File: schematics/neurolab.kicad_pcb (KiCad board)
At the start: 2 copper layers, 127 x 53.6 mm, 170 parts, among them J1 GS3, J10 GS3, J12 GS3, J13 GS3, J14 GS3, J15 GS3, J16 Channel, J17 External, J18 USB_OTG, J19 GS3, J2 GS3, J20 GS2, J21 GS2, J22 GS2, J23 GS2, J24 GS2, J25 GS2, J26 ICSP Port, J27 GS2, J28 GS2, J3 GS3, J30 GS3, J31 GS3, J32 Bluetooth, J33 Reset Select, J34 GS2, J4 GS2, J5 GS2, J6 GS3, J7 GS3, J8 PowerOut, J9 GS3, Q1 2N7002, U1 ADP1720ARMZ-5, U10 OPA2111KP, U11 AD8422ARMZ, U12 OP4117, U13 OPA2111KP, U14 AD8422ARMZ, U15 OP4117, U16 AD7173, U17 ADR445BR, U18 Arduino, U2 ADP1720ARMZ-3.3, U3 AD8475, U4 AD8475, U5 MAX7480ESA+, U6 MAX7480ESA+, U7 MAX7480ESA+, U8 MAX7480ESA+, U9 TLC555CD, Y1 FA-20H

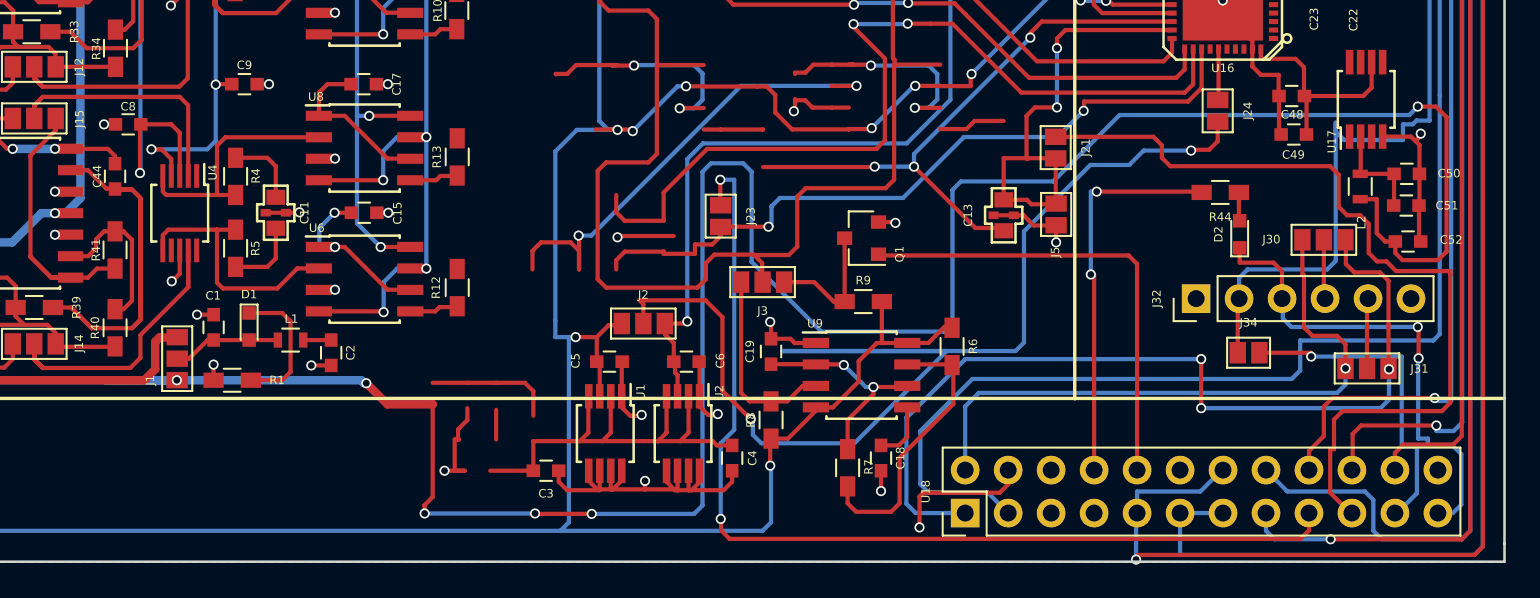
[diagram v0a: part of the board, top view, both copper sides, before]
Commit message: optimize: component placement
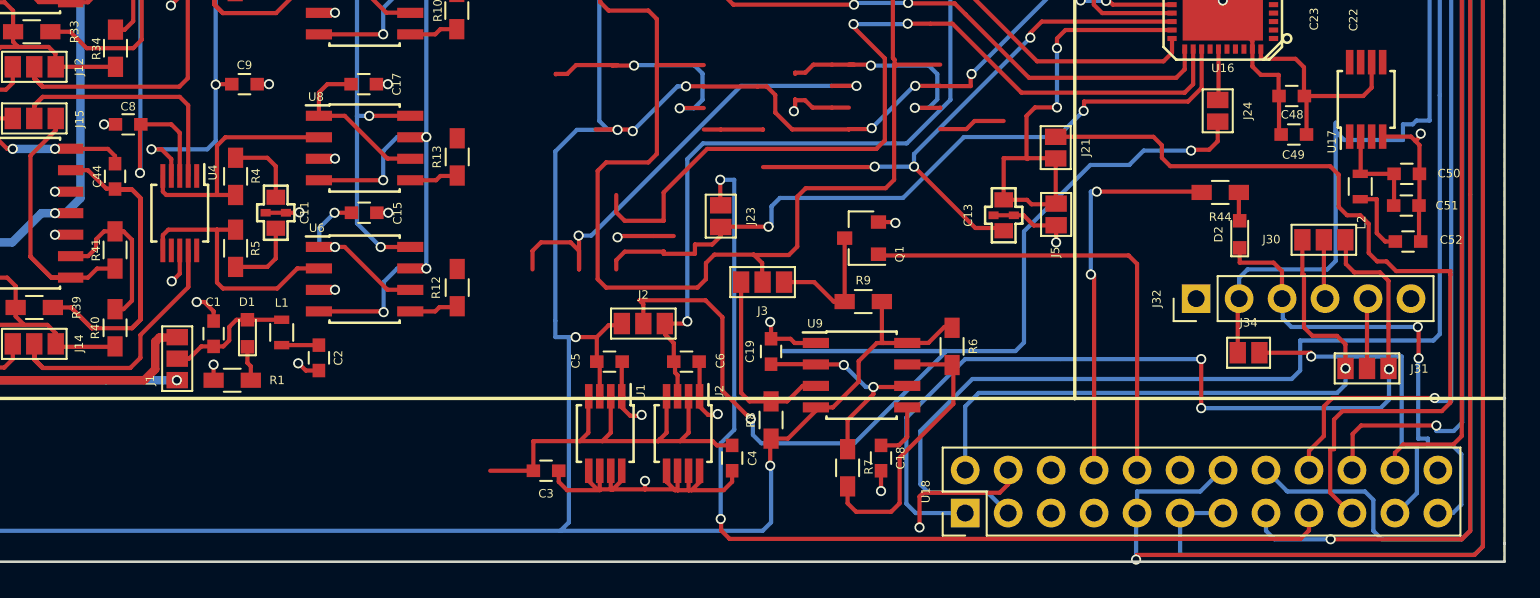
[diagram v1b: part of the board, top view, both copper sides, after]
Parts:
- moved C2 0.78 mm to (146.9, 113.8)
- moved L1 0.69 mm to (144.7, 112.3), turned to 270 degrees
- moved D1 0.41 mm to (142.7, 112.4), turned to 90 degrees
- moved C1 0.38 mm to (140.7, 112.4)
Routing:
- net +5.5V: track 187.0 -> 50.1 mm, vias 7 -> 2
- net (no net): track 140.0 -> 124.6 mm, vias 14 -> 13
- net Net-(D1-Pad1): track 8.19 -> 2.06 mm
- net Net-(C1-Pad1): track 6.41 -> 7.60 mm
- net GND: track 241.8 -> 242.9 mm
- net /External Power/VIN: track 29.4 -> 30.0 mm

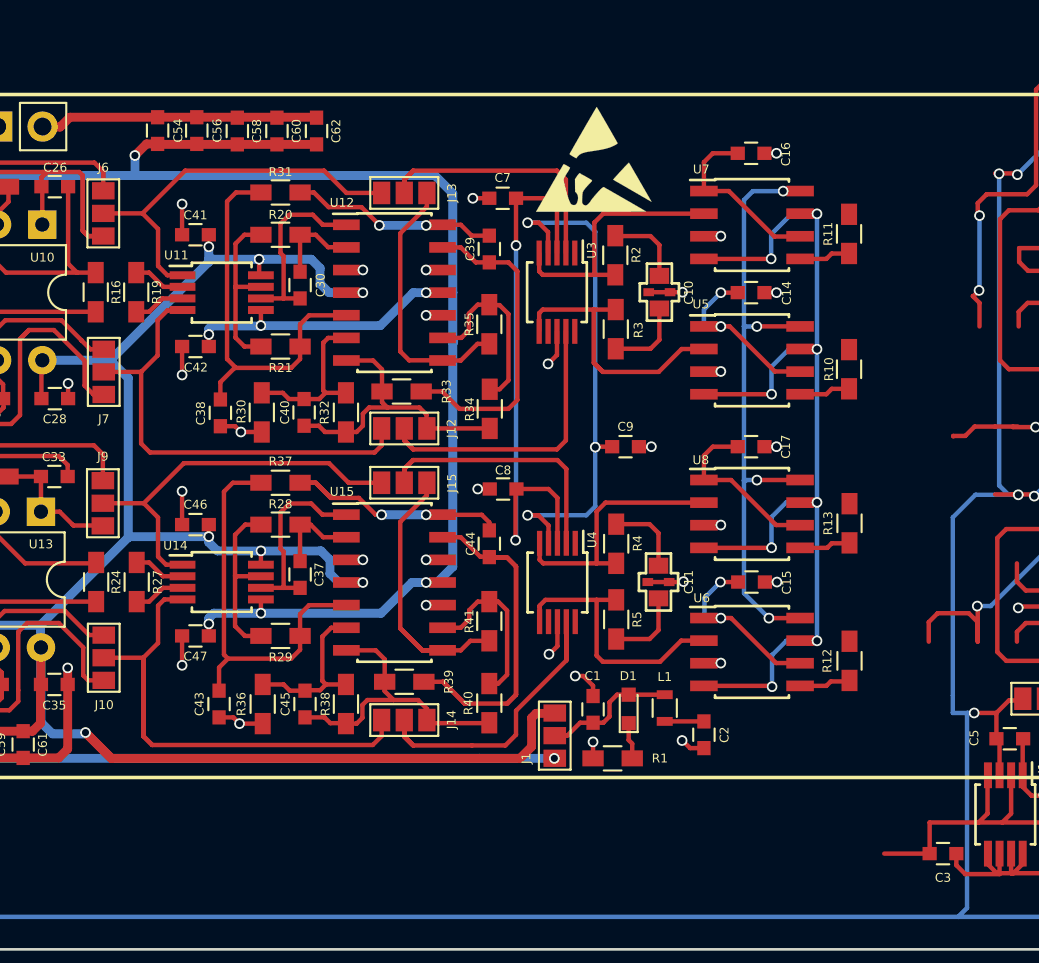
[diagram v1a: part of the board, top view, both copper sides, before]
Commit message: optimize: reduce spacing 20mils
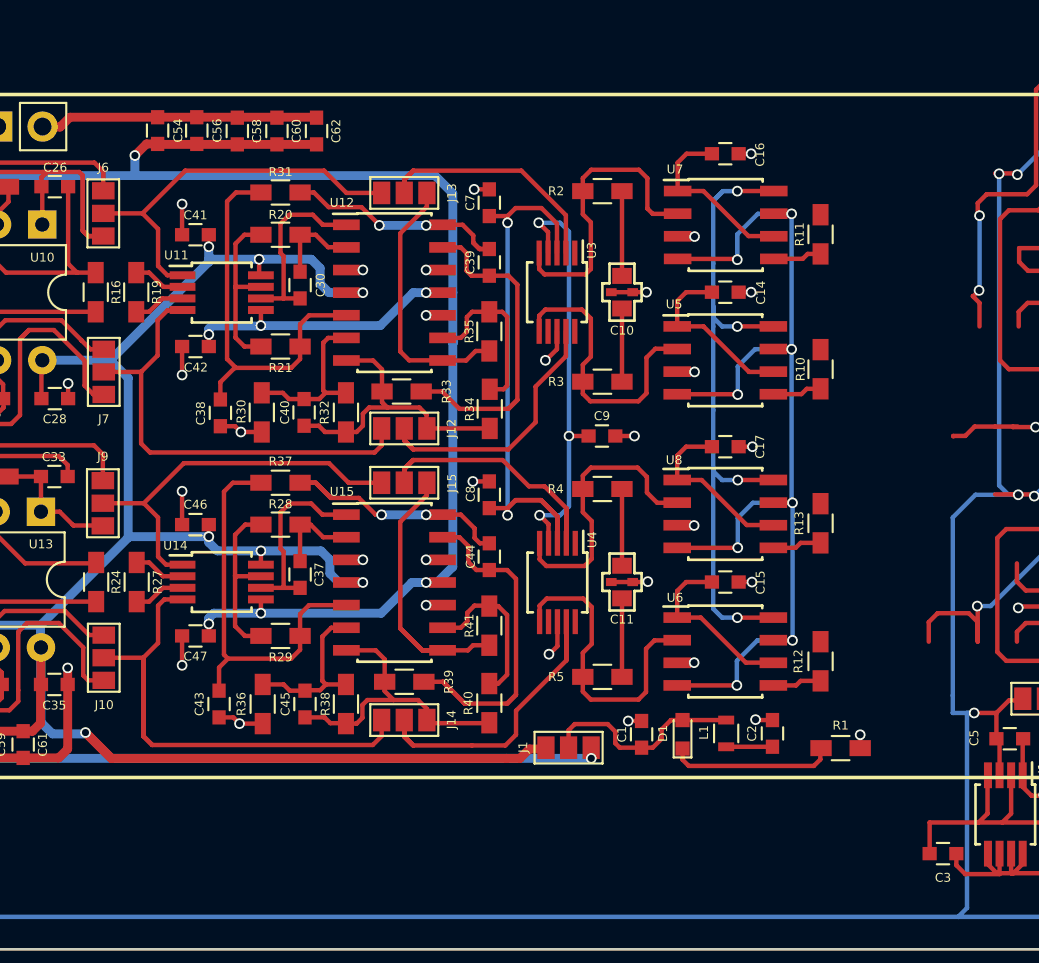
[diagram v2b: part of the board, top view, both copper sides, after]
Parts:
- removed REF***: ESD-Logo_6.6x6mm_SilkScreen, Symbols:ESD-Logo_6.6x6mm_SilkScreen
- moved R1 12.8 mm to (154.6, 114.6), turned to 0 degrees
- moved C2 3.85 mm to (150.8, 113.8), turned to 90 degrees
- moved L1 3.73 mm to (148.2, 113.8)
- moved R2 3.67 mm to (141.2, 83.3), turned to 180 degrees
- moved D1 3.34 mm to (145.7, 113.8)
- moved R5 3.32 mm to (141.2, 110.6), turned to 180 degrees
- moved R4 3.17 mm to (141.2, 100.0), turned to 180 degrees
- moved C1 3.06 mm to (143.4, 113.8)
- moved R3 3.04 mm to (141.2, 94.0), turned to 180 degrees
- moved C10 2.10 mm to (142.3, 89.0)
- moved C11 2.05 mm to (142.3, 105.2)
- moved R12 1.63 mm to (153.5, 109.7)
- moved R13 1.62 mm to (153.5, 102.0)
- moved R11 1.60 mm to (153.5, 85.7)
- moved R10 1.60 mm to (153.5, 93.3)
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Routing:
- net Net-(C44-Pad1): track 29.4 -> 20.5 mm
- net Net-(D1-Pad1): track 2.06 -> 9.33 mm
- net Net-(C9-Pad1): track 29.4 -> 24.0 mm
- net VCCIO: track 106.4 -> 110.9 mm
- net Net-(C1-Pad1): track 7.60 -> 11.8 mm
- net +5.5V: track 50.1 -> 53.4 mm
- net /Clock Block/CLK: track 134.0 -> 137.0 mm
- net /Attenuator/-IN0.4XB: track 15.9 -> 18.8 mm
- net /Attenuator/-OUTA: track 19.0 -> 16.4 mm
- net /Attenuator/-OUTB: track 15.1 -> 17.4 mm
- net +12V: track 164.2 -> 162.0 mm
- net /Attenuator/+OUTA: track 14.7 -> 16.9 mm
- net /External Power/VIN: track 30.0 -> 27.8 mm
- net Net-(C39-Pad2): track 11.7 -> 13.3 mm
- net /Attenuator/+OUTB: track 14.5 -> 15.9 mm
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
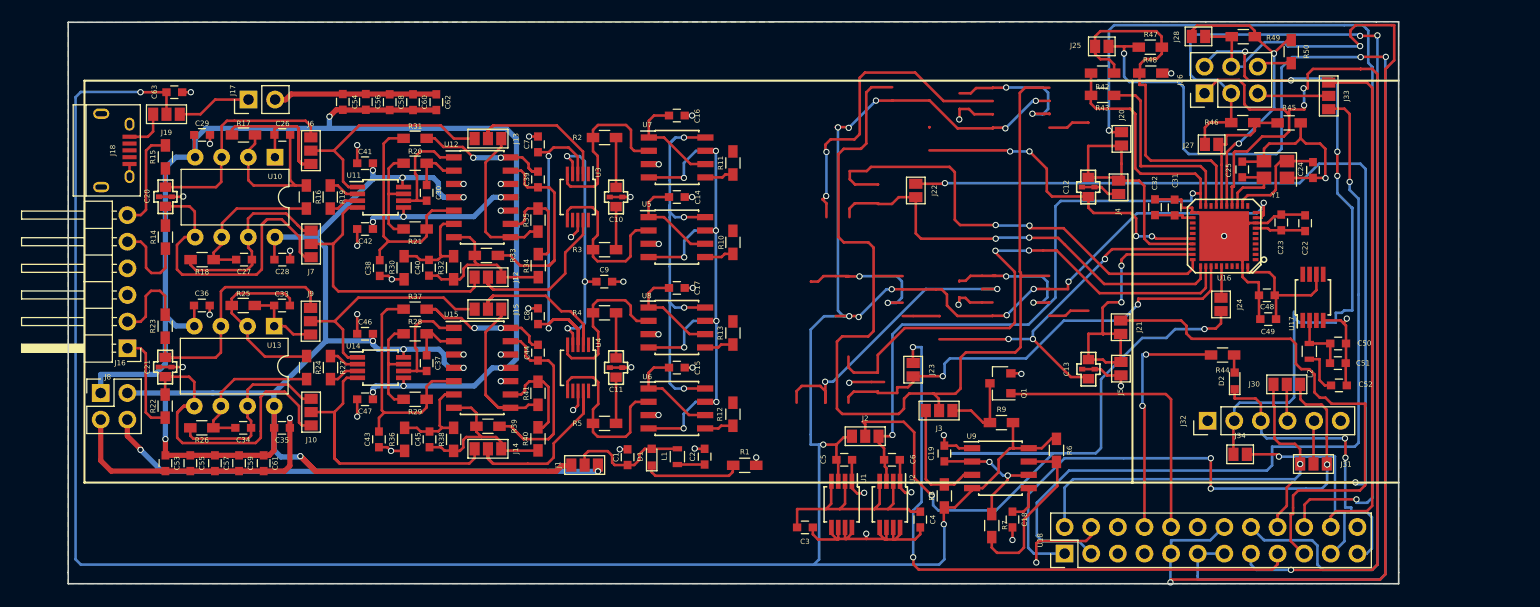
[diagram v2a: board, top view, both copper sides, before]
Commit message: optimize: redundant foot prints
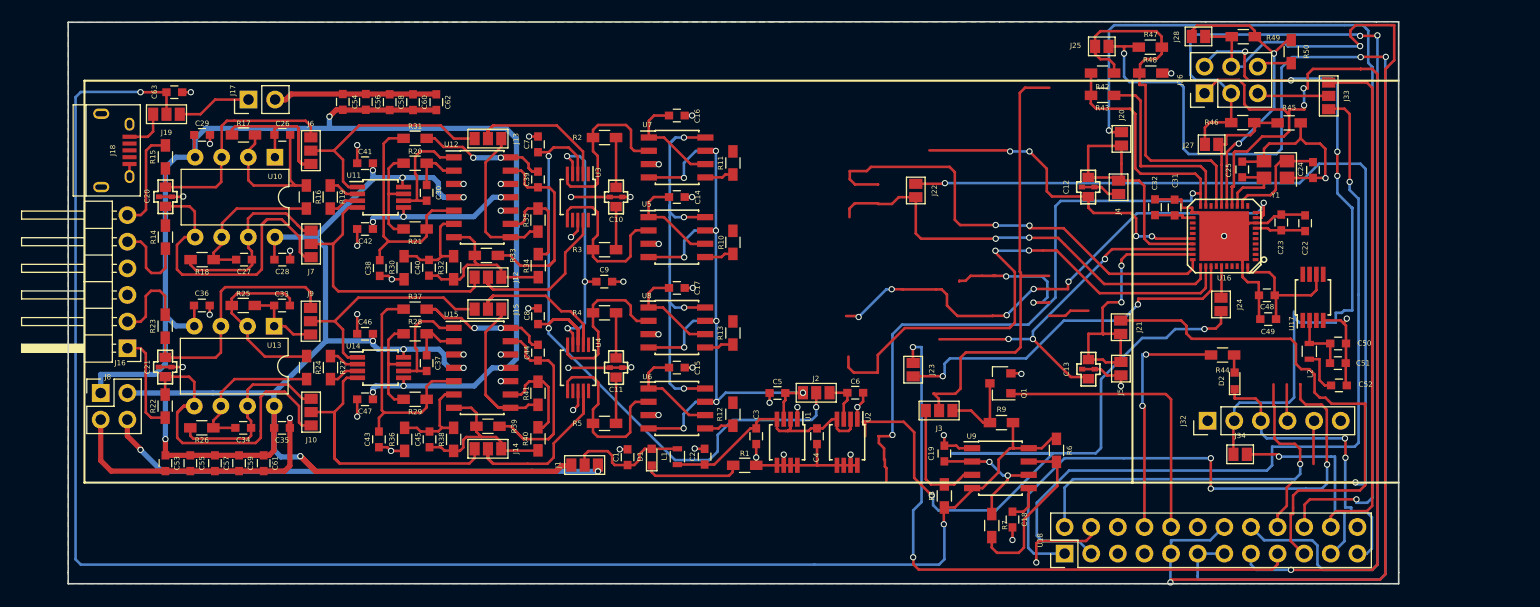
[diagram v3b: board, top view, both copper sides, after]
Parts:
- removed J30, J31: GS3, Connectors:GS3
- moved C4 12.7 mm to (161.5, 111.8)
- moved C3 9.86 mm to (155.7, 111.8), turned to 270 degrees
- moved C5 9.02 mm to (157.7, 107.7), turned to 180 degrees
- moved U1 7.88 mm to (158.7, 112.4)
- moved C6 7.29 mm to (165.2, 107.7)
- moved U2 7.19 mm to (164.4, 112.4)
- moved J2 6.25 mm to (161.4, 107.7)
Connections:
- J32 pad 4: Net-(J30-Pad2) -> TxO
- J32 pad 5: Net-(J31-Pad2) -> RxI
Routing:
- net (no net): track 124.6 -> 17.7 mm, vias 13 -> 2
- net +5V: track 352.6 -> 286.1 mm, vias 23 -> 17
- net /Clock Block/CLK: track 137.0 -> 82.7 mm
- net VCCIO: track 110.9 -> 146.8 mm, vias 4 -> 5
- net /RC Filter 1/+OUTB': track 47.8 -> 39.5 mm
- net /External Power/VIN: track 27.8 -> 23.3 mm
- net +3V: track 78.3 -> 82.7 mm
- net RxI: track 37.3 -> 41.5 mm
- net Net-(J31-Pad2): track 4.19 -> 0.00 mm
- net TxO: track 53.3 -> 56.8 mm
- net Net-(J30-Pad2): track 3.55 -> 0.00 mm
- net GND: track 242.0 -> 238.5 mm, vias 51 -> 55

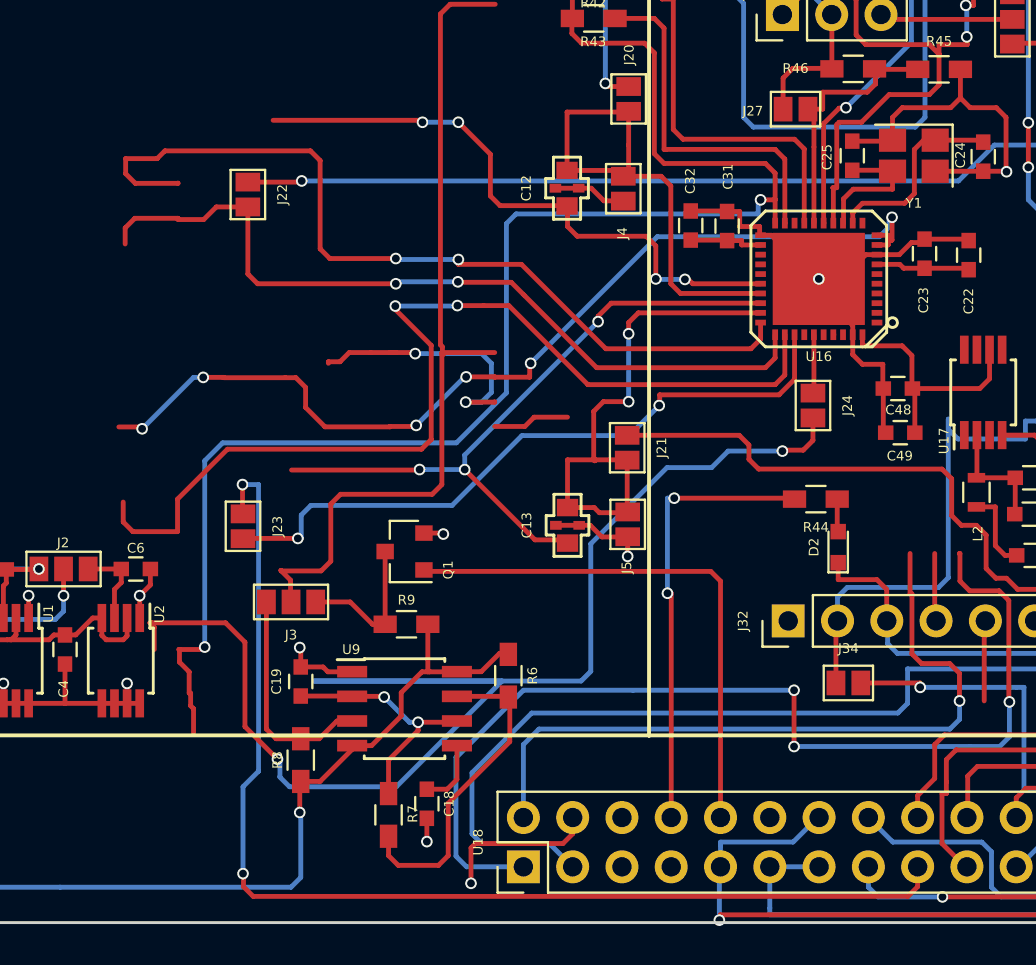
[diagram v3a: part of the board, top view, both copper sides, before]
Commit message: optimize: routing to minimize length
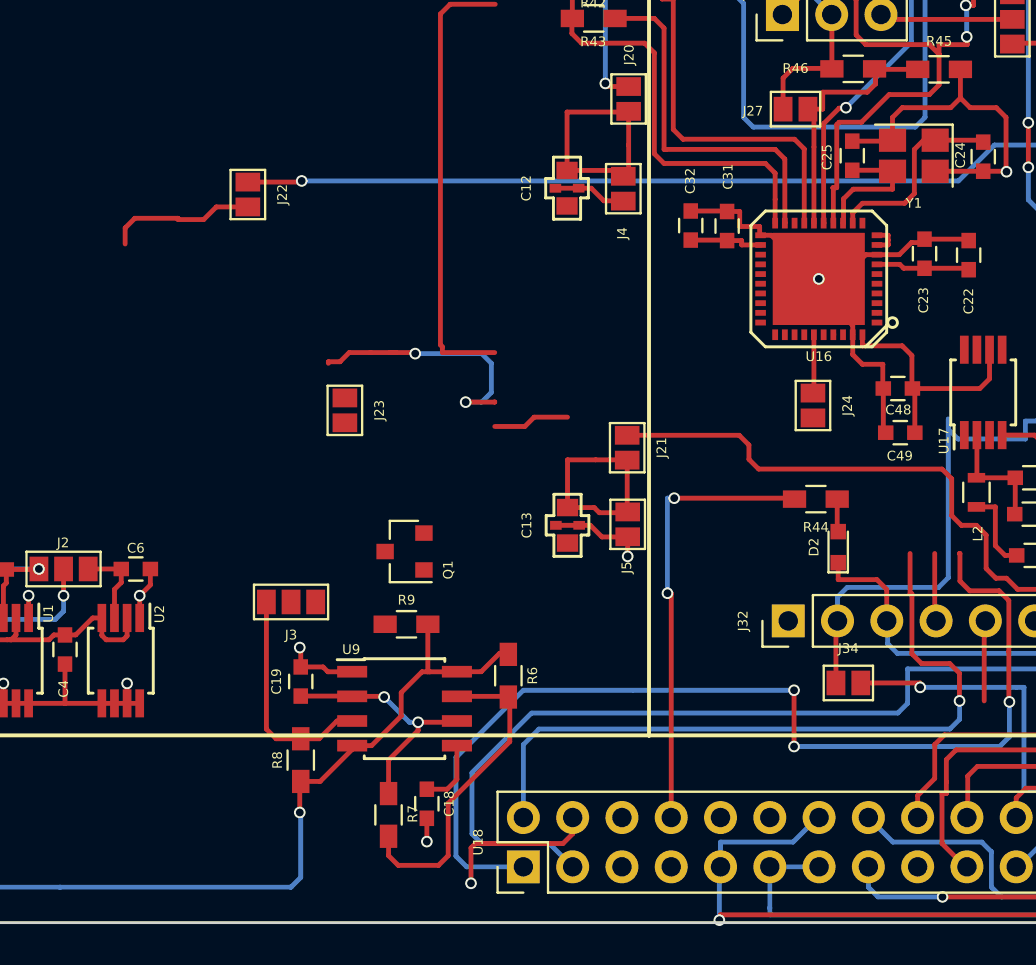
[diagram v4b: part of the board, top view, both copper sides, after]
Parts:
- moved J23 7.95 mm to (175.9, 99.5)
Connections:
- U16 pad 26: /ADConverter/AIN4 -> /ADConverter/AIN5
- U16 pad 27: /ADConverter/AIN5 -> /RC Filter 1/+OUTA'
- U16 pad 28: /ADConverter/AIN6 -> /RC Filter 1/-OUTA'
- U16 pad 29: /ADConverter/AIN7 -> /ADConverter/AIN4
- U16 pad 30: /RC Filter 1/-OUTA' -> (no net)
- U16 pad 31: /RC Filter 1/+OUTA' -> /ADConverter/AIN7
- U16 pad 32: /RC Filter 1/-OUTB' -> /RC Filter 1/+OUTB'
- U16 pad 33: /RC Filter 1/+OUTB' -> /RC Filter 1/-OUTB'
- U16 pad 34: (no net) -> /ADConverter/AIN6
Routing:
- net VCCIO: track 146.8 -> 72.7 mm, vias 5 -> 3
- net AD0: track 59.6 -> 0.00 mm, vias 2 -> 0
- net +3V: track 82.7 -> 26.4 mm, vias 2 -> 0
- net /RC Filter 1/-OUTB': track 56.2 -> 4.41 mm, vias 2 -> 0
- net +5V: track 286.1 -> 236.8 mm, vias 17 -> 11
- net /RC Filter 1/-OUTA': track 48.8 -> 4.11 mm, vias 2 -> 0
- net /Clock Block/CLK: track 82.7 -> 38.9 mm
- net /RC Filter 1/+OUTB': track 39.5 -> 4.31 mm, vias 2 -> 0
- net /ADConverter/AIN6: track 35.3 -> 0.16 mm, vias 3 -> 0
- net /RC Filter 1/+OUTA': track 46.6 -> 12.5 mm, vias 2 -> 0
- net /ADConverter/AIN4: track 31.6 -> 0.04 mm, vias 4 -> 0
- net EXCLK: track 27.8 -> 0.12 mm
- net (no net): track 17.7 -> 41.0 mm
- net /ADConverter/AIN7: track 27.2 -> 11.5 mm, vias 2 -> 0
- net /ADConverter/AIN5: track 25.6 -> 13.0 mm
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
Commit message: optimize: alternative route for +5V
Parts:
- moved J22 56.1 mm to (226.2, 97.9)
- moved J23 50.2 mm to (225.9, 103.9)
- moved C18 8.62 mm to (173.1, 114.8), turned to 180 degrees
- moved C19 7.10 mm to (167.9, 109.3)
- moved U9 7.01 mm to (173.2, 111.0)
- moved R6 6.99 mm to (178.5, 109.3)
- moved R8 6.86 mm to (167.9, 113.7)
- moved R7 6.63 mm to (178.5, 113.7), turned to 270 degrees
- moved R9 2.21 mm to (181.0, 109.3), turned to 90 degrees
- moved J3 2.10 mm to (173.2, 107.2)
- moved Q1 1.90 mm to (179.8, 105.0)
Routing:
- net AD1: track 86.1 -> 0.00 mm, vias 2 -> 0
- net +5V: track 236.8 -> 175.7 mm, vias 11 -> 13
- net /Clock Block/CLK: track 38.9 -> 83.7 mm, vias 4 -> 5
- net (no net): track 41.0 -> 0.00 mm, vias 2 -> 0
- net Net-(R6-Pad2): track 16.7 -> 4.91 mm
- net Net-(J3-Pad3): track 0.00 -> 9.88 mm
- net /RC Filter 1/+OUTA': track 12.5 -> 4.76 mm
- net GND: track 237.5 -> 238.6 mm, vias 54 -> 53
- net Net-(J3-Pad1): track 11.6 -> 10.6 mm
- net Net-(C19-Pad1): track 13.1 -> 14.0 mm
